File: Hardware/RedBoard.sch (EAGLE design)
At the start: 75 parts, among them IC3 LM1117, J2 ISP, J3 5.5x2.1mm Barrel, J4 QWIIC_RIGHT_ANGLE, J5 USB Female Type C Connector, Q1 20V/4.2A/52mΩ/1.4W, Q2 310mA/60V/1.6Ω, Q3 310mA/60V/1.6Ω, U3 3.3V, U4 ATMEGA328P_TQFP, U5 CH340C, Y1 16MHz

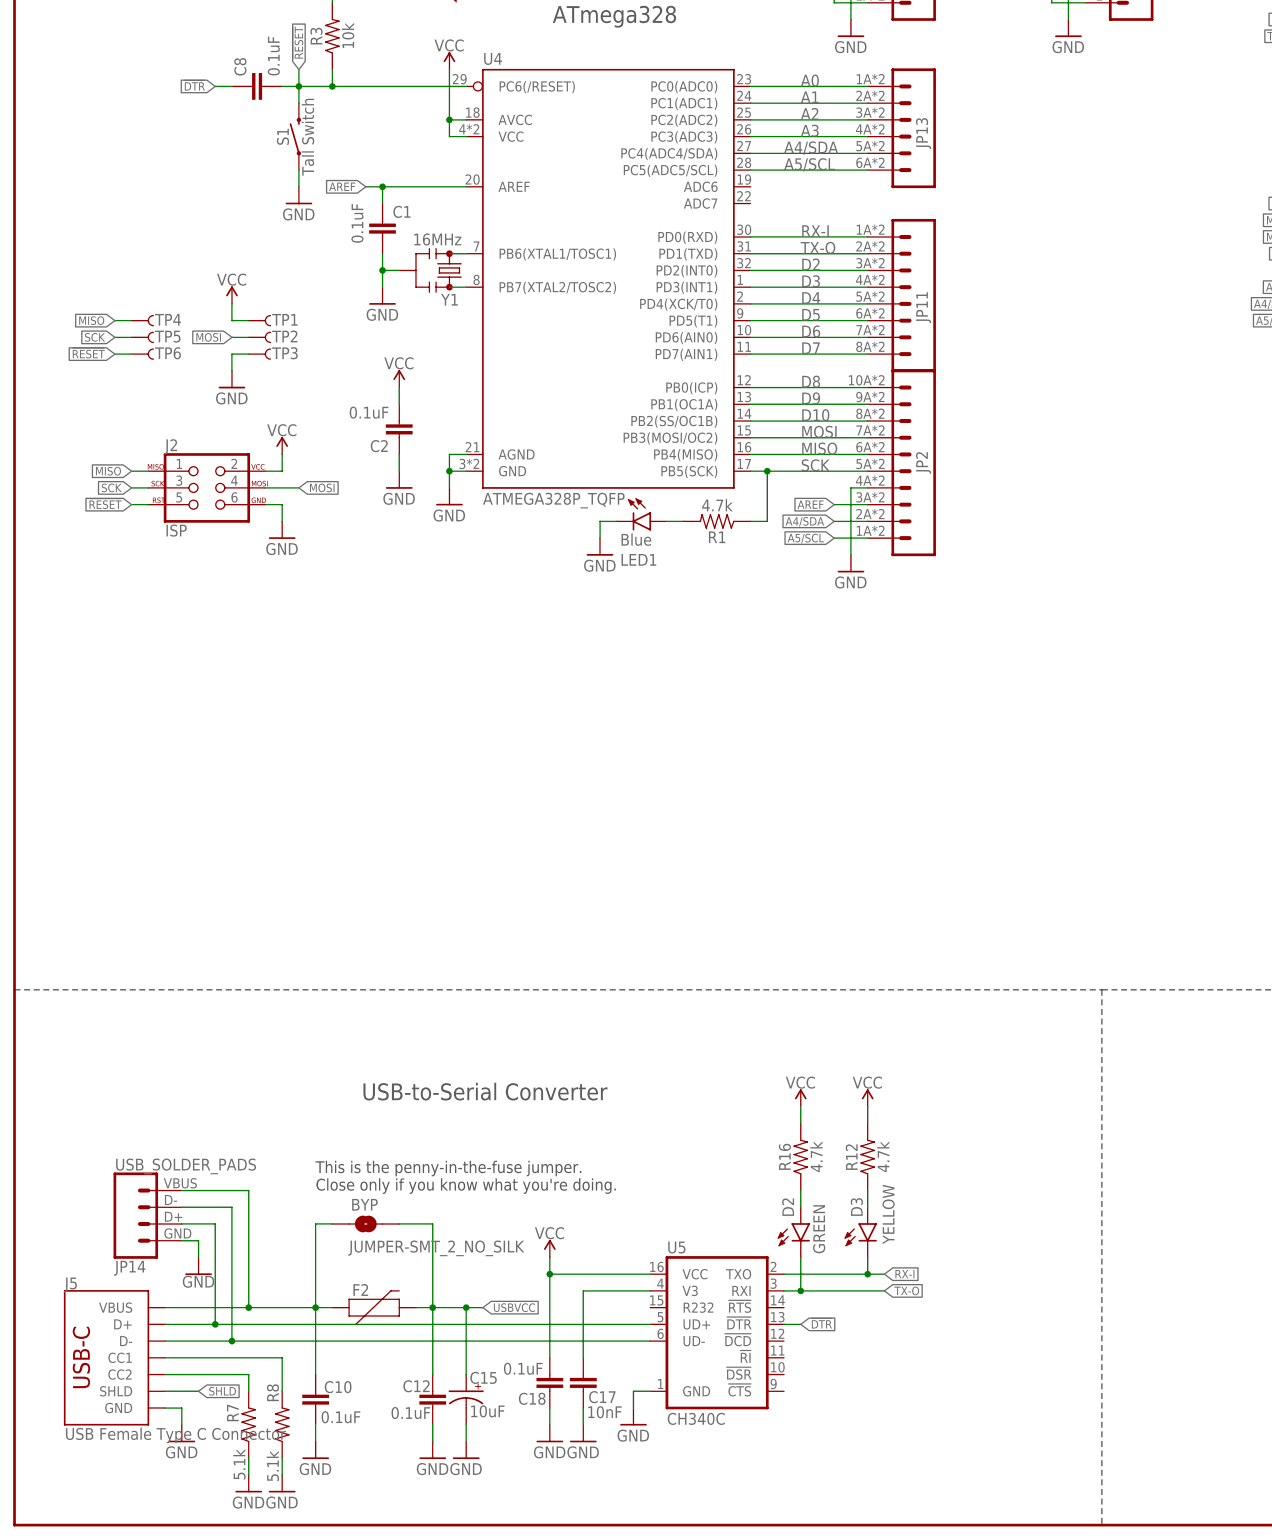
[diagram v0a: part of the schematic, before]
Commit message: Rename files to "RedBoard"
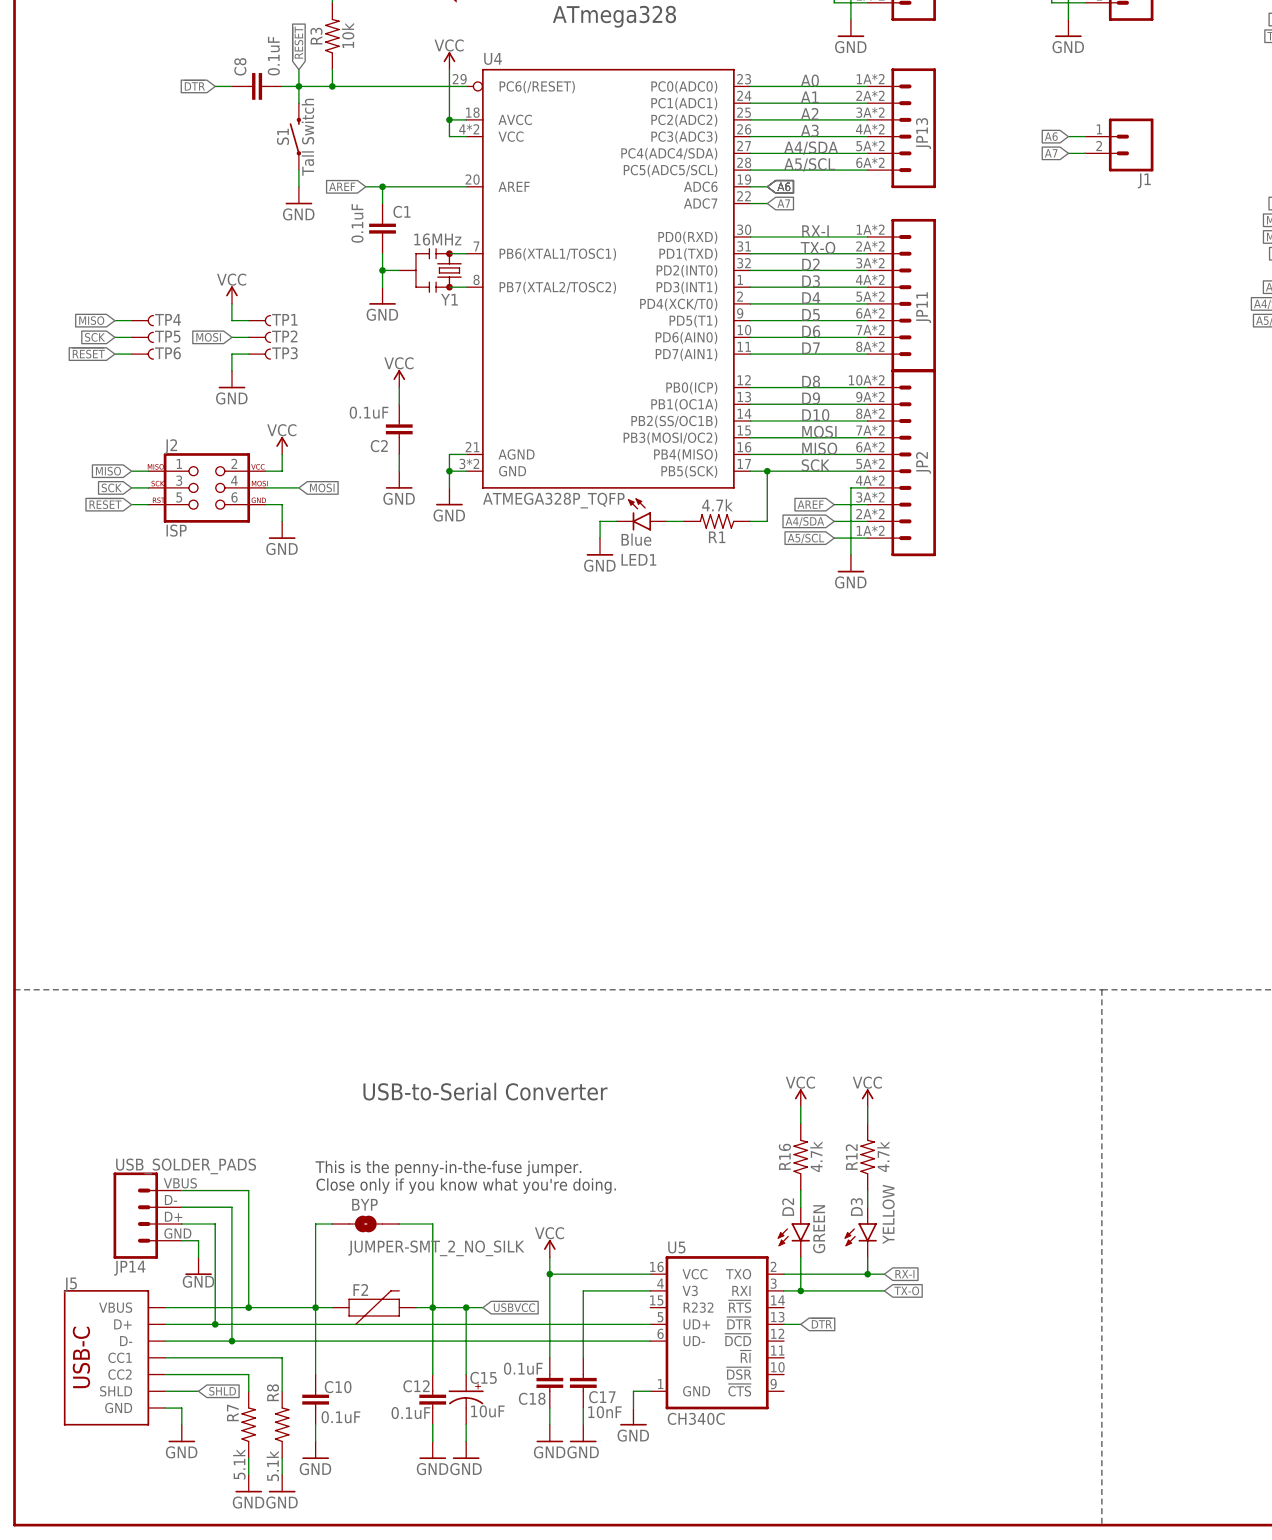
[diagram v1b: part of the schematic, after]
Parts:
- added J1: (no value), SparkFun-Connectors:CONN_021X02_NO_SILK
- J5: device SparkFun-Connectors:USB_C_4-LAYER-ISOLATED -> SparkFun-Connectors:USB_C_2-LAYER_PADS
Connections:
- new net A6: J1.1, U4.ADC6
- new net A7: J1.2, U4.ADC7
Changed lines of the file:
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@@
 <part name="SUPPLY12" library="SparkFun-PowerSymbols" deviceset="VCC" device=""/>
 <part name="SUPPLY21" library="SparkFun-PowerSymbols" deviceset="VCC" device=""/>
-<part name="J5" library="SparkFun-Connectors" deviceset="USB_C" device="_4-LAYER-ISOLATED" value="USB Female Type C Connector"/>
+<part name="J5" library="SparkFun-Connectors" deviceset="USB_C" device="_2-LAYER_PADS" value="USB Female Type C Connector"/>
 <part name="GND38" library="SparkFun-PowerSymbols" deviceset="GND" device=""/>
 <part name="U5" library="SparkFun-IC-Comms" deviceset="CH340C" device=""/>
@@
 <part name="SUPPLY9" library="SparkFun-PowerSymbols" deviceset="3.3V" device=""/>
 <part name="GND9" library="SparkFun-PowerSymbols" deviceset="GND" device=""/>
+<part name="J1" library="SparkFun-Connectors" deviceset="CONN_02" device="1X02_NO_SILK"/>
 </parts>
 <sheets>
@@
 </instance>
 <instance part="J5" gate="J1" x="10.16" y="25.4" smashed="yes">
-<attribute name="VALUE" x="7.62" y="12.954" size="1.778" layer="96" font="vector" rot="MR180" align="top-left"/>
 <attribute name="NAME" x="7.62" y="35.814" size="1.778" layer="95" font="vector"/>
 </instance>
@@
 <instance part="GND9" gate="1" x="246.38" y="233.68" smashed="yes">
 <attribute name="VALUE" x="246.38" y="233.426" size="1.778" layer="96" align="top-center"/>
+</instance>
+<instance part="J1" gate="G$1" x="170.18" y="210.82" smashed="yes" rot="R180">
+<attribute name="VALUE" x="172.72" y="215.646" size="1.778" layer="96" font="vector" rot="R180"/>
+<attribute name="NAME" x="172.72" y="205.232" size="1.778" layer="95" font="vector" rot="R180"/>
 </instance>
 </instances>
@@
 </segment>
 </net>
+<net name="A6" class="0">
+<segment>
+<pinref part="J1" gate="G$1" pin="1"/>
+<wire x1="162.56" y1="210.82" x2="160.02" y2="210.82" width="0.1524" layer="91"/>
+<label x="160.02" y="210.82" size="1.27" layer="95" rot="R180" xref="yes"/>
+</segment>
+<segment>
+<pinref part="U4" gate="U1" pin="ADC6"/>
+<wire x1="111.76" y1="203.2" x2="114.3" y2="203.2" width="0.1524" layer="91"/>
+<label x="114.3" y="203.2" size="1.27" layer="95" xref="yes"/>
+<label x="114.3" y="203.2" size="1.27" layer="95" xref="yes"/>
+<label x="114.3" y="203.2" size="1.27" layer="95" xref="yes"/>
+</segment>
+</net>
+<net name="A7" class="0">
+<segment>
+<pinref part="J1" gate="G$1" pin="2"/>
+<wire x1="162.56" y1="208.28" x2="160.02" y2="208.28" width="0.1524" layer="91"/>
+<label x="160.02" y="208.28" size="1.27" layer="95" rot="R180" xref="yes"/>
+</segment>
+<segment>
+<pinref part="U4" gate="U1" pin="ADC7"/>
+<wire x1="111.76" y1="200.66" x2="114.3" y2="200.66" width="0.1524" layer="91"/>
+<label x="114.3" y="200.66" size="1.27" layer="95" xref="yes"/>
+</segment>
+</net>

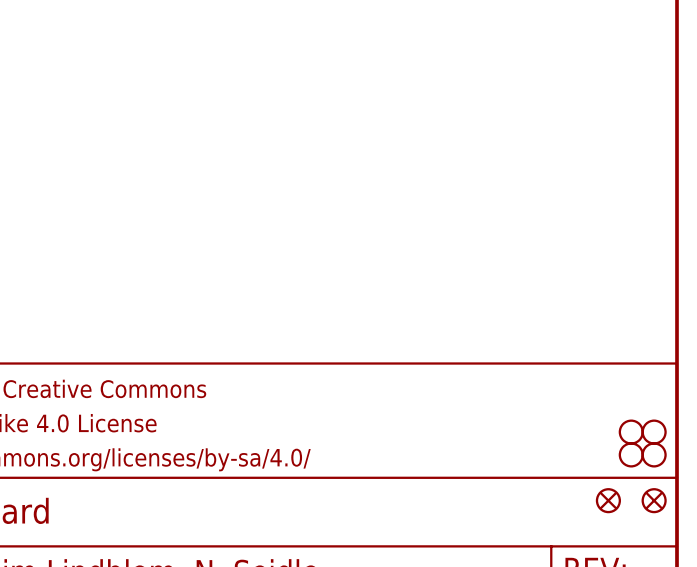
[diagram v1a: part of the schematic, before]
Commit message: Finished vectorizing redboard logo. Updated board files
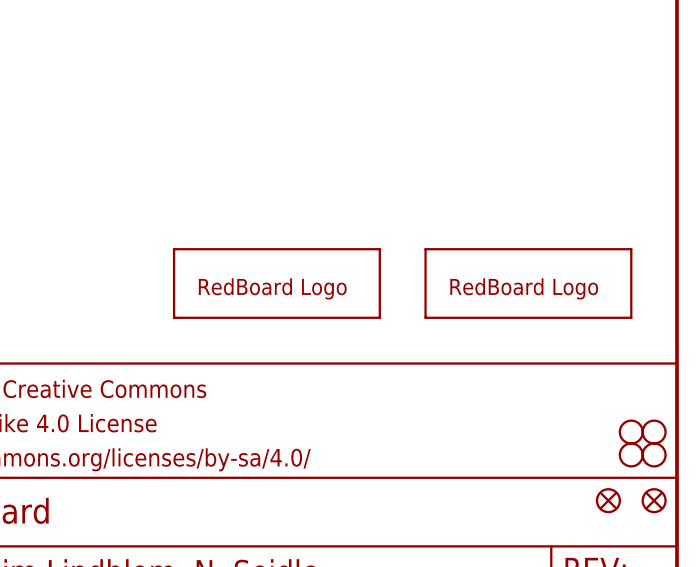
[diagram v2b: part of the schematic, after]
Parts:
- added U$1, U$78: REDBOARD_LOGO, redboard_logo:REDBOARD_LOGO
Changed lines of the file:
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@@
 <?xml version="1.0" encoding="utf-8"?>
 <!DOCTYPE eagle SYSTEM "eagle.dtd">
-<eagle version="9.5.2">
+<eagle version="9.6.2">
 <drawing>
 <settings>
@@
 <part name="GND9" library="SparkFun-PowerSymbols" deviceset="GND" device=""/>
 <part name="J1" library="SparkFun-Connectors" deviceset="CONN_02" device="1X02_NO_SILK"/>
+<part name="U$78" library="redboard_logo" deviceset="REDBOARD_LOGO" device=""/>
+<part name="U$1" library="redboard_logo" deviceset="REDBOARD_LOGO" device=""/>
 </parts>
 <sheets>
@@
 <attribute name="NAME" x="172.72" y="205.232" size="1.778" layer="95" font="vector" rot="R180"/>
 </instance>
+<instance part="U$78" gate="G$1" x="403.86" y="40.64" smashed="yes"/>
+<instance part="U$1" gate="G$1" x="375.92" y="40.64" smashed="yes"/>
 </instances>
 <busses>

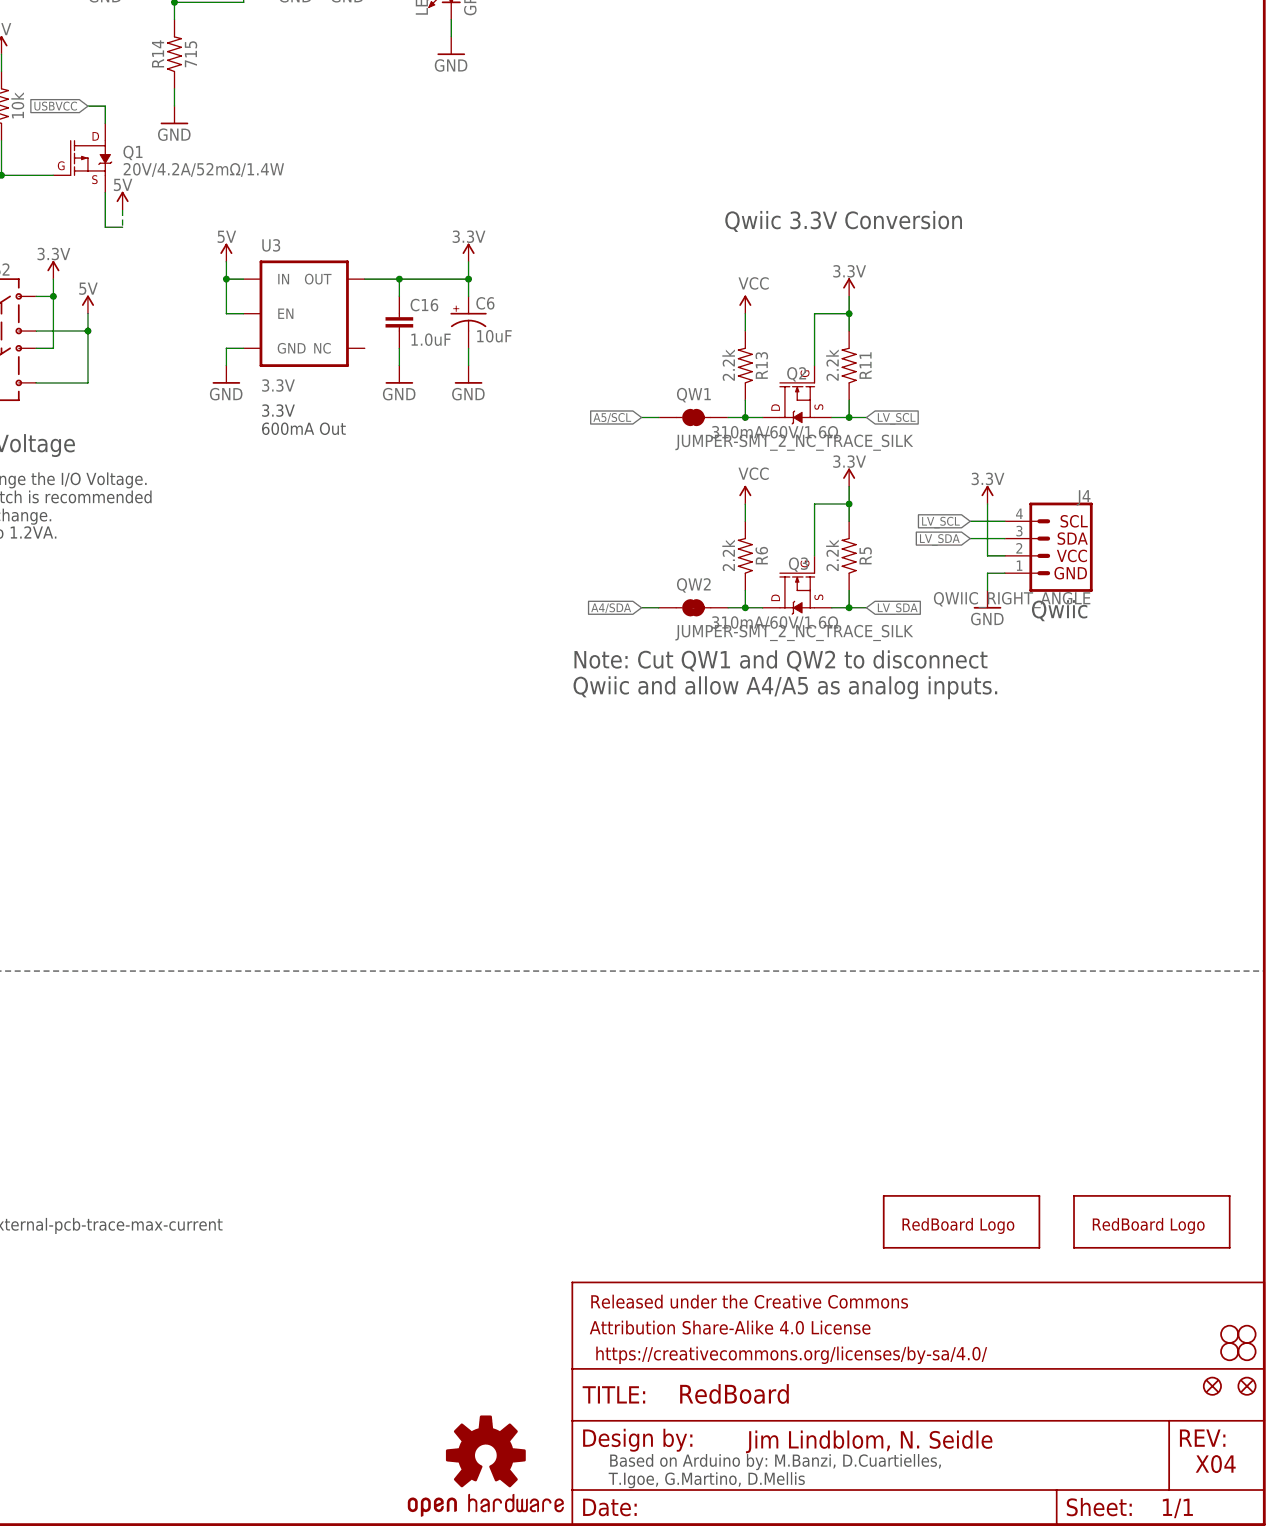
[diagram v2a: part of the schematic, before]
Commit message: Ran schematic and board auto-checklists
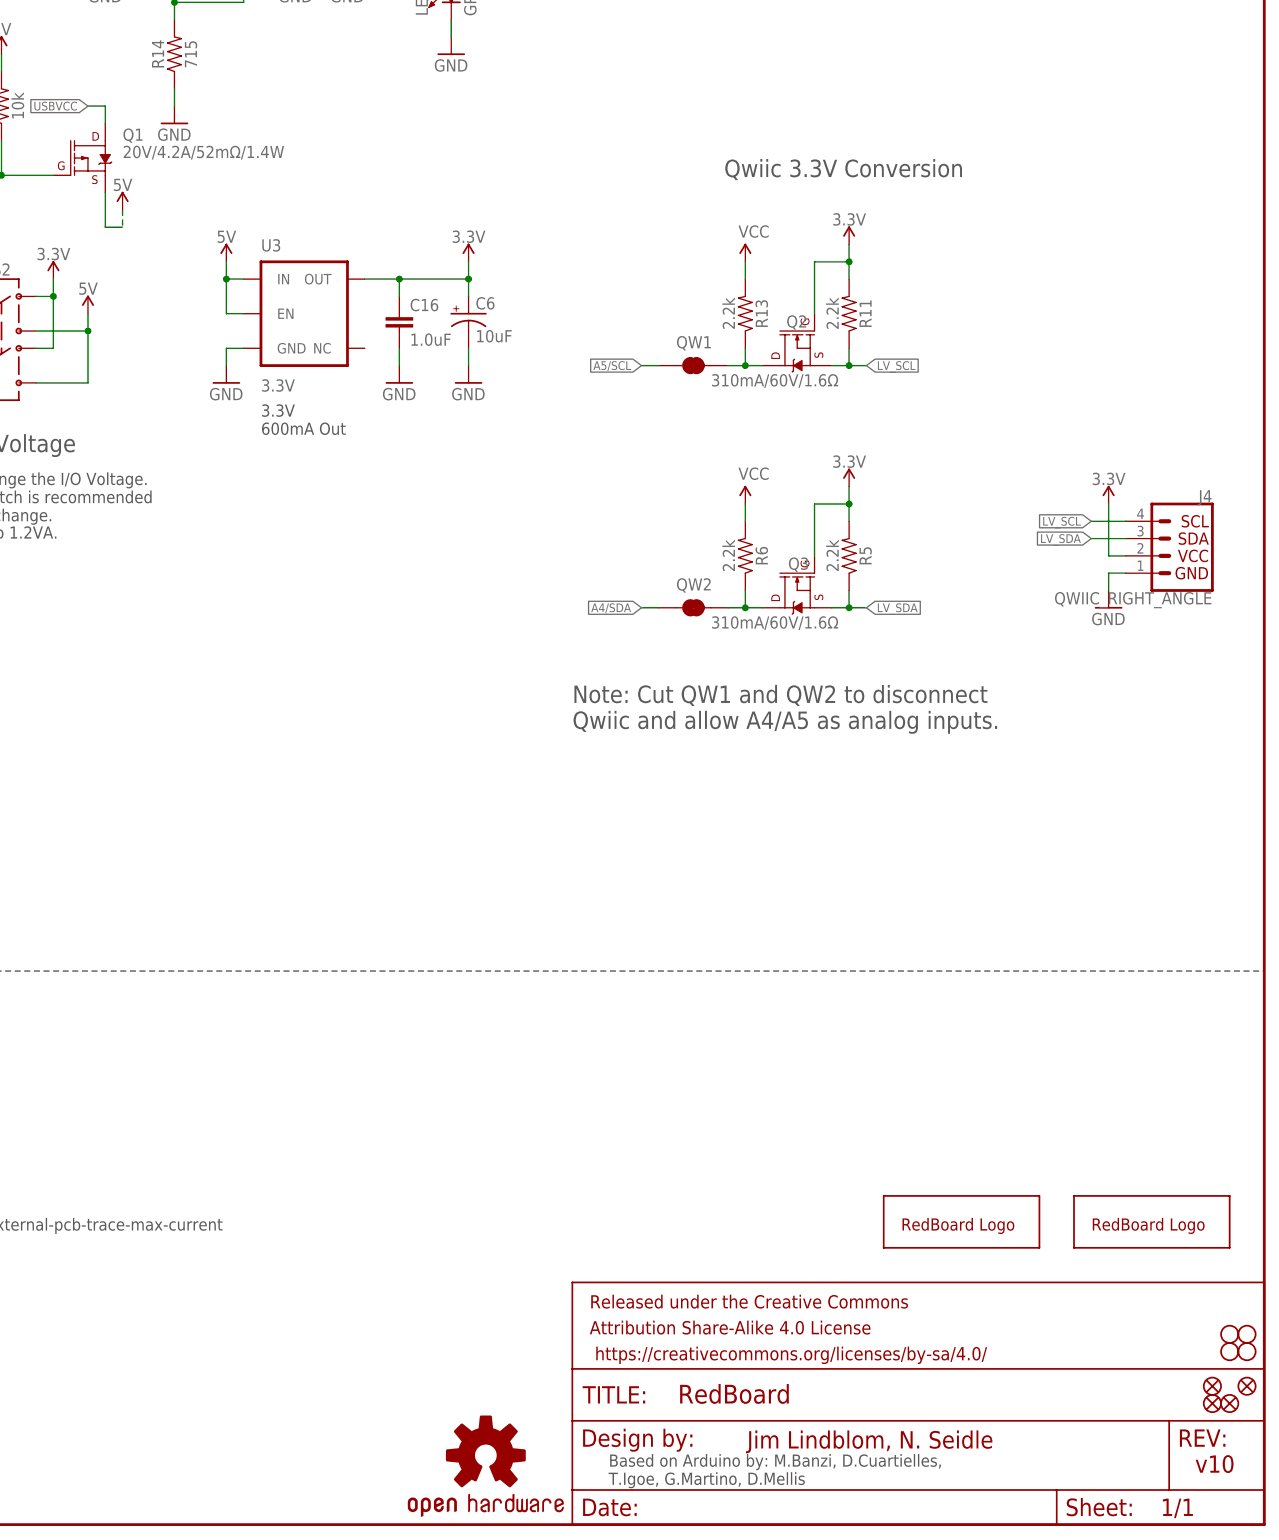
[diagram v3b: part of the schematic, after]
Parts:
- added FD1, FD2: FIDUCIAL1X2, SparkFun-Aesthetics:FIDUCIAL1X2
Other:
- note added: "v10"
- note removed: "Qwiic"
- note removed: "X04"
- moved on the sheet: J4, Q2, QW1, R11, R13
